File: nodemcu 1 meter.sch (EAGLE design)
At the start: 16 parts, among them K1 SRD-05VDC-SL-C, T1 BC547, U1 ZC563900, U2 78L05

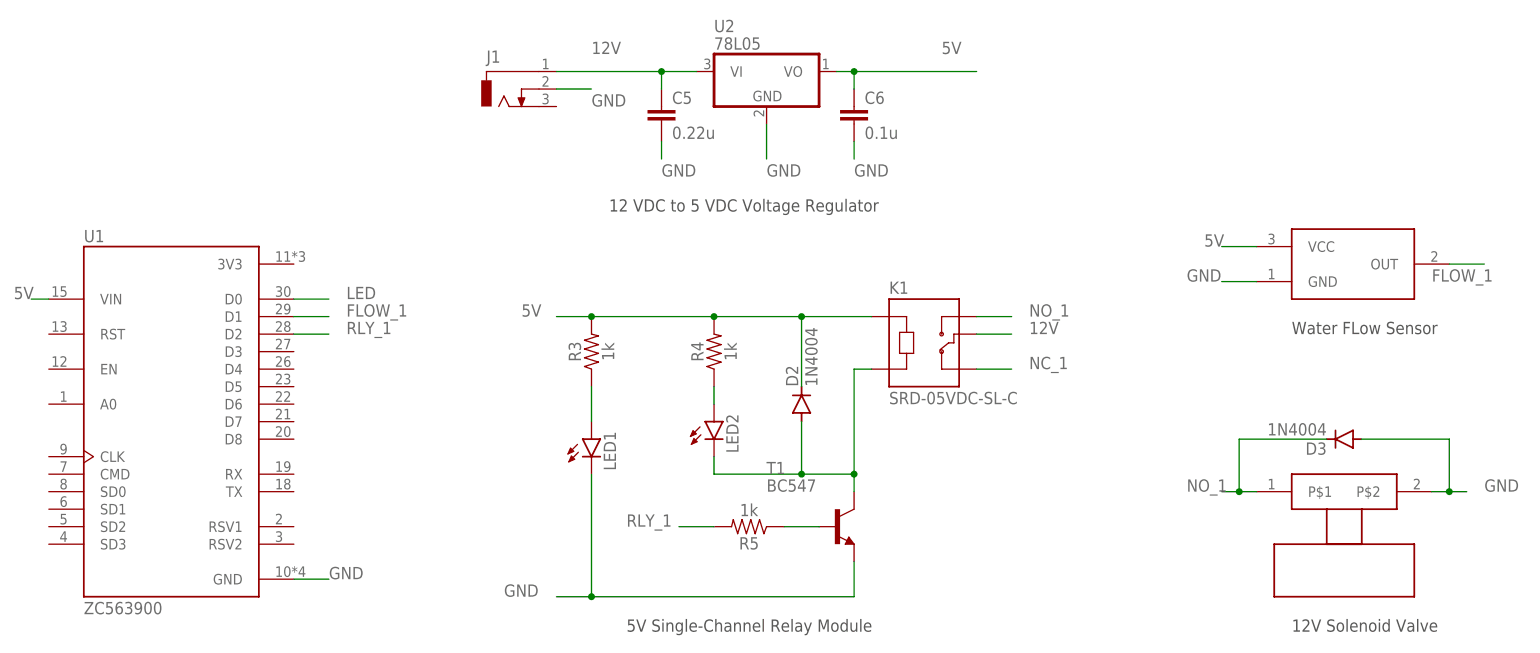
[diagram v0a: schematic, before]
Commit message: Board design and eagle sch upload
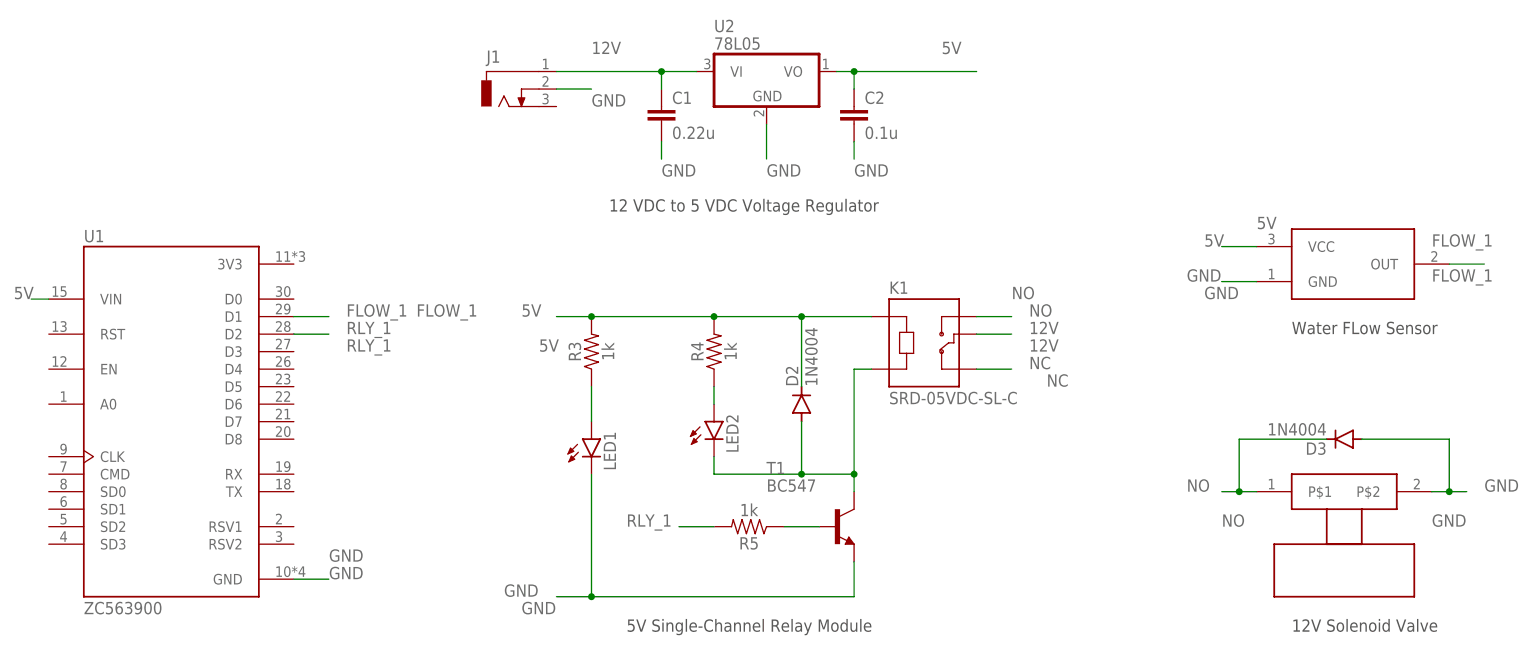
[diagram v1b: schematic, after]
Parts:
- renumbered C5 to C1, C6 to C2
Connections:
- net NC_1 renamed NC
- net NO_1 renamed NO
- removed net LED: U1.D0
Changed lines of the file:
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@@
 <setting verticaltext="up"/>
 </settings>
-<grid distance="0.1" unitdist="inch" unit="inch" style="dots" multiple="1" display="yes" altdistance="0.01" altunitdist="inch" altunit="inch"/>
+<grid distance="0.1" unitdist="inch" unit="inch" style="lines" multiple="1" display="no" altdistance="0.01" altunitdist="inch" altunit="inch"/>
 <layers>
 <layer number="1" name="Top" color="4" fill="1" visible="no" active="no"/>
@@
 <part name="D3" library="diode" library_urn="urn:adsk.eagle:library:210" deviceset="1N4004" device="" package3d_urn="urn:adsk.eagle:package:43336/1"/>
 <part name="U2" library="linear" deviceset="78LXXZ" device="" value="78L05"/>
-<part name="C5" library="rcl" deviceset="C-EU" device="025-025X050" value="0.22u"/>
-<part name="C6" library="rcl" deviceset="C-EU" device="025-025X050" value="0.1u"/>
+<part name="C1" library="rcl" deviceset="C-EU" device="025-025X050" value="0.22u"/>
+<part name="C2" library="rcl" deviceset="C-EU" device="025-025X050" value="0.1u"/>
 <part name="J1" library="con-jack" library_urn="urn:adsk.eagle:library:154" deviceset="DCJ0303" device="" package3d_urn="urn:adsk.eagle:package:7493/1"/>
 </parts>
@@
 <attribute name="VALUE" x="119.38" y="84.455" size="1.778" layer="96"/>
 </instance>
-<instance part="C5" gate="G$1" x="111.76" y="76.2" smashed="yes">
+<instance part="C1" gate="G$1" x="111.76" y="76.2" smashed="yes">
 <attribute name="NAME" x="113.284" y="76.581" size="1.778" layer="95"/>
 <attribute name="VALUE" x="113.284" y="71.501" size="1.778" layer="96"/>
 </instance>
-<instance part="C6" gate="G$1" x="139.7" y="76.2" smashed="yes">
+<instance part="C2" gate="G$1" x="139.7" y="76.2" smashed="yes">
 <attribute name="NAME" x="141.224" y="76.581" size="1.778" layer="95"/>
 <attribute name="VALUE" x="141.224" y="71.501" size="1.778" layer="96"/>
@@
 <junction x="101.6" y="5.08"/>
 <label x="88.9" y="5.08" size="1.778" layer="95"/>
+<label x="91.44" y="2.54" size="1.778" layer="95"/>
 </segment>
 <segment>
@@
 <wire x1="58.42" y1="7.62" x2="63.5" y2="7.62" width="0.1524" layer="91"/>
 <label x="63.5" y="7.62" size="1.778" layer="95"/>
+<label x="63.5" y="10.16" size="1.778" layer="95"/>
 </segment>
 <segment>
@@
 <wire x1="198.12" y1="50.8" x2="193.04" y2="50.8" width="0.1524" layer="91"/>
 <label x="187.96" y="50.8" size="1.778" layer="95"/>
+<label x="190.5" y="48.26" size="1.778" layer="95"/>
 </segment>
 <segment>
@@
 <junction x="226.06" y="20.32"/>
 <label x="231.14" y="20.32" size="1.778" layer="95"/>
+<label x="223.52" y="15.24" size="1.778" layer="95"/>
 </segment>
 <segment>
@@
 </segment>
 <segment>
-<pinref part="C5" gate="G$1" pin="1"/>
+<pinref part="C1" gate="G$1" pin="1"/>
 <wire x1="111.76" y1="71.12" x2="111.76" y2="68.58" width="0.1524" layer="91"/>
 <label x="111.76" y="66.04" size="1.778" layer="95"/>
@@
 </segment>
 <segment>
-<pinref part="C6" gate="G$1" pin="1"/>
+<pinref part="C2" gate="G$1" pin="1"/>
 <wire x1="139.7" y1="71.12" x2="139.7" y2="68.58" width="0.1524" layer="91"/>
 <label x="139.7" y="66.04" size="1.778" layer="95"/>
@@
 <wire x1="198.12" y1="55.88" x2="193.04" y2="55.88" width="0.1524" layer="91"/>
 <label x="190.5" y="55.88" size="1.778" layer="95"/>
+<label x="198.12" y="58.42" size="1.778" layer="95"/>
 </segment>
 <segment>
@@
 <junction x="101.6" y="45.72"/>
 <label x="91.44" y="45.72" size="1.778" layer="95"/>
+<label x="93.98" y="40.64" size="1.778" layer="95"/>
 </segment>
 <segment>
@@
 <label x="152.4" y="83.82" size="1.778" layer="95"/>
 <pinref part="U2" gate="A1" pin="VO"/>
-<pinref part="C6" gate="G$1" pin="2"/>
+<pinref part="C2" gate="G$1" pin="2"/>
 </segment>
 </net>
@@
 <wire x1="157.48" y1="43.18" x2="162.56" y2="43.18" width="0.1524" layer="91"/>
 <label x="165.1" y="43.18" size="1.778" layer="95"/>
+<label x="165.1" y="40.64" size="1.778" layer="95"/>
 </segment>
 <segment>
@@
 <pinref part="U2" gate="A1" pin="VI"/>
 <wire x1="96.52" y1="81.28" x2="111.76" y2="81.28" width="0.1524" layer="91"/>
-<pinref part="C5" gate="G$1" pin="2"/>
+<pinref part="C1" gate="G$1" pin="2"/>
 <wire x1="111.76" y1="81.28" x2="116.84" y2="81.28" width="0.1524" layer="91"/>
 <wire x1="111.76" y1="78.74" x2="111.76" y2="81.28" width="0.1524" layer="91"/>
@@
 </segment>
 </net>
-<net name="LED" class="0">
-<segment>
-<pinref part="U1" gate="G$1" pin="D0"/>
-<wire x1="58.42" y1="48.26" x2="63.5" y2="48.26" width="0.1524" layer="91"/>
-<label x="66.04" y="48.26" size="1.778" layer="95"/>
-</segment>
-</net>
 <net name="FLOW_1" class="0">
 <segment>
@@
 <wire x1="58.42" y1="45.72" x2="63.5" y2="45.72" width="0.1524" layer="91"/>
 <label x="66.04" y="45.72" size="1.778" layer="95"/>
+<label x="76.2" y="45.72" size="1.778" layer="95"/>
 </segment>
 <segment>
@@
 <wire x1="226.06" y1="53.34" x2="231.14" y2="53.34" width="0.1524" layer="91"/>
 <label x="223.52" y="50.8" size="1.778" layer="95"/>
+<label x="223.52" y="55.88" size="1.778" layer="95"/>
 </segment>
 </net>
@@
 <wire x1="58.42" y1="43.18" x2="63.5" y2="43.18" width="0.1524" layer="91"/>
 <label x="66.04" y="43.18" size="1.778" layer="95"/>
-</segment>
-</net>
-<net name="NO_1" class="0">
+<label x="66.04" y="40.64" size="1.778" layer="95"/>
+</segment>
+</net>
+<net name="NO" class="0">
 <segment>
 <pinref part="VALVE1" gate="G$1" pin="P$1"/>
@@
 <wire x1="195.58" y1="27.94" x2="195.58" y2="20.32" width="0.1524" layer="91"/>
 <junction x="195.58" y="20.32"/>
+<label x="193.04" y="15.24" size="1.778" layer="95"/>
 </segment>
 <segment>
@@
 <wire x1="157.48" y1="45.72" x2="162.56" y2="45.72" width="0.1524" layer="91"/>
 <label x="165.1" y="45.72" size="1.778" layer="95"/>
-</segment>
-</net>
-<net name="NC_1" class="0">
+<label x="162.56" y="48.26" size="1.778" layer="95"/>
+</segment>
+</net>
+<net name="NC" class="0">
 <segment>
 <pinref part="K1" gate="G$1" pin="NC"/>
 <wire x1="157.48" y1="38.1" x2="162.56" y2="38.1" width="0.1524" layer="91"/>
 <label x="165.1" y="38.1" size="1.778" layer="95"/>
+<label x="167.64" y="35.56" size="1.778" layer="95"/>
 </segment>
 </net>
@@
 </sheet>
 </sheets>
+<errors>
+</errors>
 </schematic>
 </drawing>
